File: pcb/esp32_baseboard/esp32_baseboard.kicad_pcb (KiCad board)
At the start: 2 copper layers, 225 x 132 mm, 42 parts, among them J1 Screw_12V_IN, J10 LIM_MIN_NC, J11 LIM_MAX_NC, J12 LIM_MIN_NC, J13 LIM_MAX_NC, J14 BUP_30S, J15 BUZZER_5V, J16 AOD4184, J17 TFT_TOUCH, J18 EC11_ENC, J2 NEMA17_OUT, J4 OPTO_FIELD_IN, J5 GA12_N20, J6 GA12_N20, J7 GA12_N20, J8 LIM_MIN_NC, J9 LIM_MAX_NC, U1 ESP32_S3_DevKitC_1, U2 MP1584_5V3A, U3 TMC2209, U4 PC817_4CH, U5 DRV8871_Module, U6 DRV8871_Module, U7 DRV8871_Module, U9 PC817_4CH

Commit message: tmp
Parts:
- moved J5 213.6 mm to (265.0, 98.0), turned to 180 degrees
- moved J2 182.8 mm to (228.0, 65.8), turned to 180 degrees
- moved J6 166.3 mm to (265.0, 124.0), turned to 180 degrees
- moved J4 135.8 mm to (115.0, 132.0)
- moved J7 130.0 mm to (265.0, 150.0), turned to 180 degrees
- moved J11 62.0 mm to (61.0, 72.0)
- moved U3 50.0 mm to (247.0, 62.0)
- moved J10 46.0 mm to (69.0, 72.0)
- moved J14 45.2 mm to (200.0, 58.0)
- moved R1 45.2 mm to (190.0, 66.1)
- moved C20 44.3 mm to (247.0, 78.0)
- moved C23 37.2 mm to (253.0, 159.0)
- moved J15 36.7 mm to (145.0, 58.0)
- moved C22 36.2 mm to (253.0, 133.0)
- moved U9 36.1 mm to (163.0, 141.0)
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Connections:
- net /BLOWER renamed BLOWER
- net /BLW_RET renamed BLW_RET
- net /DC1_IN1 renamed DC1_IN1
- net /DC1_IN2 renamed DC1_IN2
- net /DC2_IN1 renamed DC2_IN1
- net /DC2_IN2 renamed DC2_IN2
- net /DC3_IN1 renamed DC3_IN1
- net /DC3_IN2 renamed DC3_IN2
- net /DIR renamed DIR
- net /ENC_B renamed ENC_B
- net /EN_TMC renamed EN_TMC
- net /MotA1 renamed MotA1
- net /MotA2 renamed MotA2
- net /MotB1 renamed MotB1
- net /MotB2 renamed MotB2
- net /MotDC1_A renamed MotDC1_A
- net /MotDC1_B renamed MotDC1_B
- net /MotDC2_A renamed MotDC2_A
- net /MotDC2_B renamed MotDC2_B
- net /MotDC3_A renamed MotDC3_A
- net /MotDC3_B renamed MotDC3_B
- net /OPTO_IN1 renamed OPTO_IN1
- net /OPTO_IN2 renamed OPTO_IN2
- net /OPTO_IN3 renamed OPTO_IN3
- net /OPTO_IN4 renamed OPTO_IN4
- net /OPTO_IN5 renamed OPTO_IN5
- net /OPTO_IN6 renamed OPTO_IN6
- net /OPTO_IN7 renamed OPTO_IN7
- net /OPTO_IN8 renamed OPTO_IN8
- net /OPTO_OUT1 renamed OPTO_OUT1
- net /OPTO_OUT2 renamed OPTO_OUT2
- net /OPTO_OUT3 renamed OPTO_OUT3
- net /OPTO_OUT4 renamed OPTO_OUT4
- net /OPTO_OUT5 renamed OPTO_OUT5
- net /OPTO_OUT6 renamed OPTO_OUT6
- net /OPTO_OUT7 renamed OPTO_OUT7
- net /OPTO_OUT8 renamed OPTO_OUT8
- net /OPTO_VCC_I renamed OPTO_VCC_I
- net /STEP renamed STEP
- net /TFT_BL renamed TFT_BL
- net /TFT_CS renamed TFT_CS
- net /TFT_DC renamed TFT_DC
- net /TFT_MISO renamed TFT_MISO
- net /TFT_MOSI renamed TFT_MOSI
- net /TFT_RST renamed TFT_RST
- net /TFT_SCK renamed TFT_SCK
- net /T_CS renamed T_CS
- J14 pad 4: (no net) -> unconnected-(J14-CTRL-Pad4)
- J15 pad 3: /BUZZER -> BUZZER
- J18 pad 3: /ENC_A -> ENC_A
- U1 pad 15: /ENC_A -> BUZZER
- U1 pad 24: (no net) -> unconnected-(U1-TX0-Pad24)
- U1 pad 25: (no net) -> unconnected-(U1-RX0-Pad25)
- U1 pad 3: (no net) -> unconnected-(U1-RST-Pad3)
- U1 pad 32: /BUZZER -> ENC_A
- U1 pad 33: (no net) -> unconnected-(U1-IO37-Pad33)
- U1 pad 34: (no net) -> unconnected-(U1-IO36-Pad34)
- U1 pad 35: (no net) -> unconnected-(U1-IO35-Pad35)
- U1 pad 36: (no net) -> unconnected-(U1-IO0-Pad36)
- U1 pad 41: (no net) -> unconnected-(U1-IO20-Pad41)
- U1 pad 42: (no net) -> unconnected-(U1-IO19-Pad42)
- U3 pad 2: (no net) -> unconnected-(U3-MS1-Pad2)
- U3 pad 3: (no net) -> unconnected-(U3-MS2-Pad3)
- U3 pad 4: (no net) -> unconnected-(U3-PDN-Pad4)
- U3 pad 5: (no net) -> unconnected-(U3-PDN2-Pad5)
- U3 pad 6: (no net) -> unconnected-(U3-CLK-Pad6)
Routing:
- net GND: track 1179.7 -> 780.9 mm
- net TFT_MOSI: track 437.6 -> 61.2 mm
- net MotB1: track 378.9 -> 11.4 mm
- net OPTO_VCC_I: track 474.9 -> 111.9 mm
- net TFT_SCK: track 423.0 -> 61.2 mm
- net BLOWER: track 359.9 -> 72.5 mm, vias 0 -> 1
- net OPTO_IN7: track 412.5 -> 162.8 mm
- net MotDC3_B: track 255.0 -> 10.3 mm
- net OPTO_IN8: track 275.1 -> 42.1 mm
- net MotDC3_A: track 197.0 -> 8.00 mm
- net +5V: track 0.00 -> 142.2 mm
- net OPTO_IN1: track 270.5 -> 129.8 mm
- net +3V3: track 278.4 -> 417.2 mm, vias 0 -> 2
- net TFT_RST: track 0.00 -> 133.9 mm, vias 0 -> 2
- net DC3_IN2: track 0.00 -> 119.6 mm
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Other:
- board size 225 x 132 mm -> 235 x 132 mm
- net class Default removed
- net class Power removed
- board text added: "1 POWER J1/F1/D1/U2"
- board text added: "3 TMC U3"
- board text added: "5 DRV U5-U7"
- board text added: "B STEP J2 -> U3"
- board text added: "D FIELD J4"
- board text added: "E DC MOT J5-J7"
- board text added: "F LIMIT truc 1-2 (-> U4)"
- board text added: "F LIMIT truc 3 (-> U9)"
- board text added: "G BLW J16"
- board text added: "GND 3V3 A=IO38 B=IO41"
- board text added: "J5 GA12-N20 TRUC1"
- board text added: "J6 GA12-N20 TRUC2"
- board text added: "J7 GA12-N20 TRUC3"
- board text added: "T1 J8 MIN"
- board text added: "T1 J9 MAX"
- board text added: "T2 J10 MIN"
- board text added: "T2 J11 MAX"
- board text added: "T3 J12 MIN"
- board text added: "T3 J13 MAX"
- board text added: "TOP 235x132 — giac canh module dieu khien no"
- board text added: "U5 DRV8871 GA12 VM=12V"
- board text added: "U6 DRV8871 GA12 VM=12V"
- board text added: "U7 DRV8871 GA12 VM=12V"
- board text removed: "1 POWER J1/U2"
- board text removed: "3 TMC"
- board text removed: "B STEP"
- board text removed: "B.Cu bus"
- board text removed: "D SENSE"
- board text removed: "E+F DC MOT + LIMIT (cap truc)"
- board text removed: "G BLW"
- board text removed: "GND 3V3 A=IO9 B=IO41"
- board text removed: "J5 MOT J8 MIN J9 MAX"
- board text removed: "J6 MOT J10 MIN J11 MAX"
- board text removed: "J7 MOT J12 MIN J13 MAX"
- board text removed: "TOP 225x132 — giac theo nhom | BOTTOM module"
- board text removed: "TRUC1 MOT+LIM NC"
- board text removed: "TRUC2 MOT+LIM NC"
- board text removed: "TRUC3 MOT+LIM NC"
- board text removed: "U5 DRV8871 GA12"
- board text removed: "U6 DRV8871 GA12"
- board text removed: "U7 DRV8871 GA12"
- board text removed: "VM=12V"

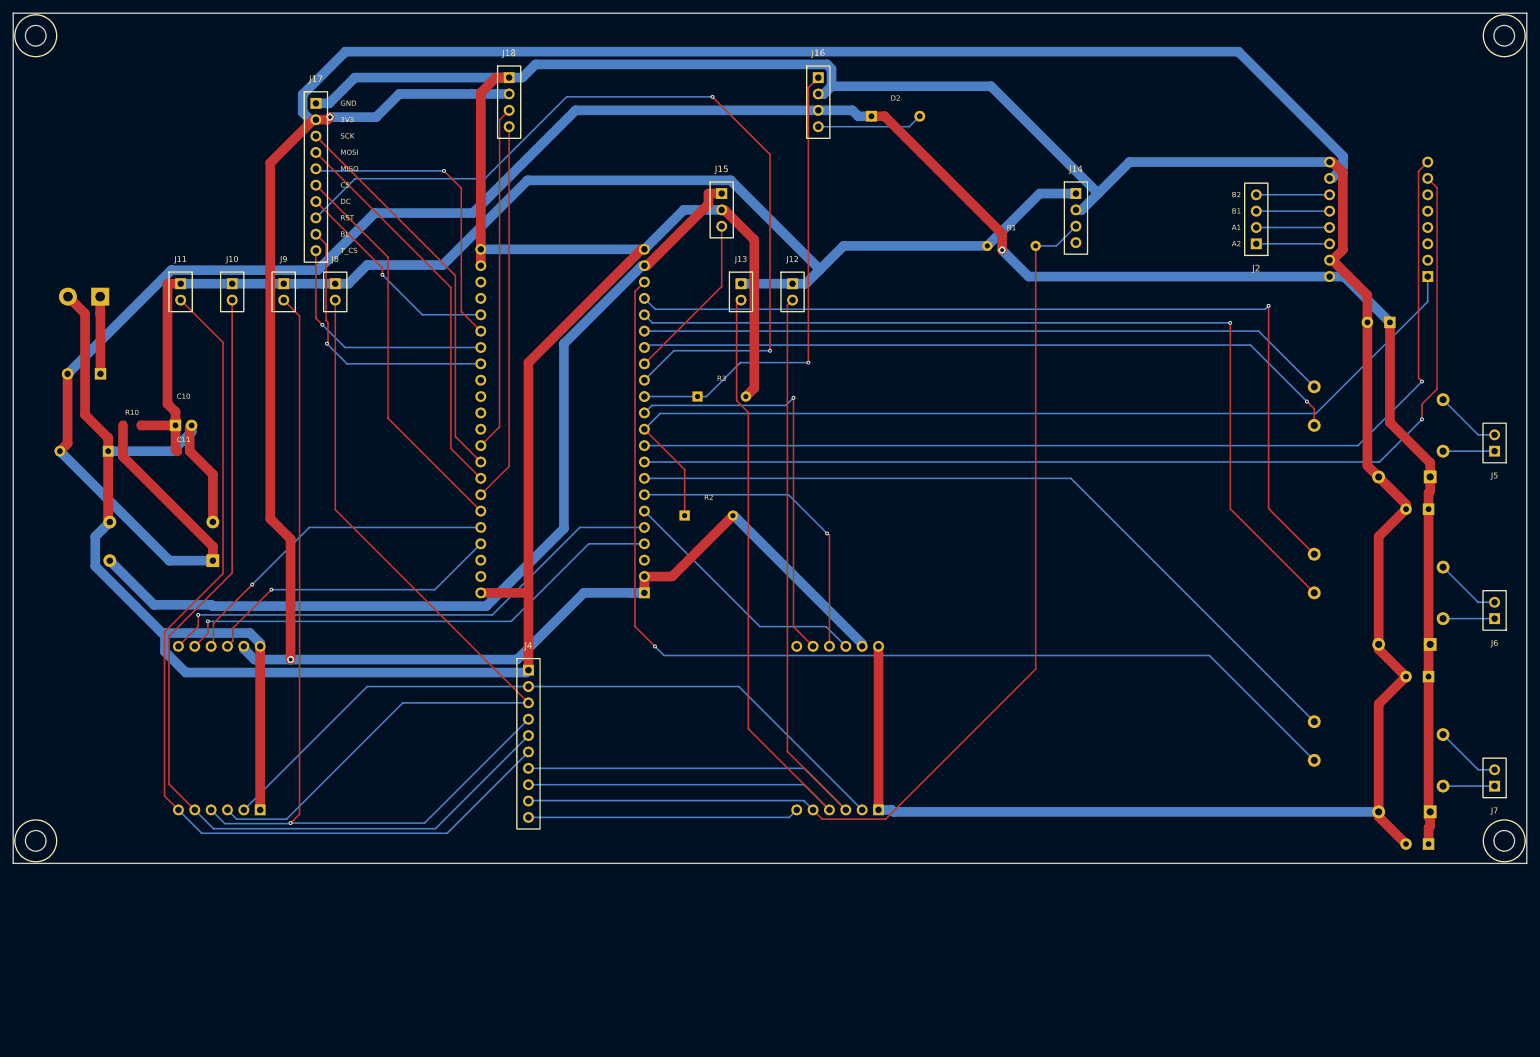
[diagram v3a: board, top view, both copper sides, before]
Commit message: sắp xếp và chọn lại linh kiện cho PCB
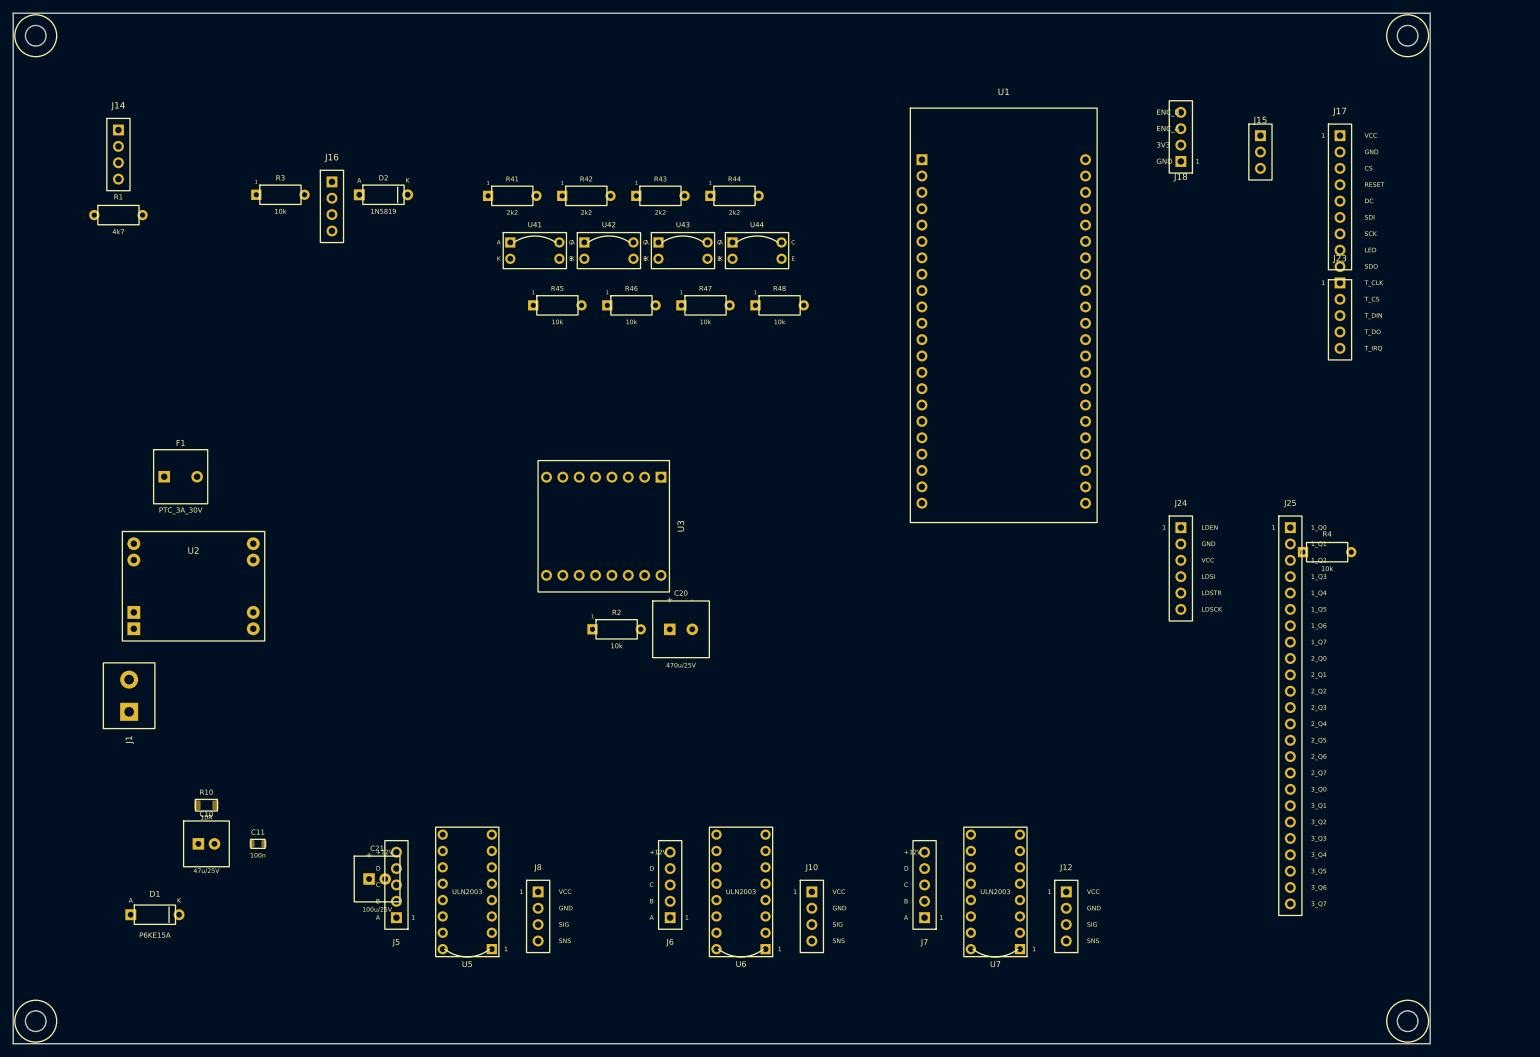
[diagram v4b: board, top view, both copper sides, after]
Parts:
- removed C22, C23: 470u/25V, ESP32_Carrier:CP_Radial_D8_470u_25V
- removed J11, J13, J9: LIM_MAX_NC, ESP32_Carrier:PinHeader_1x02_LimitSW
- removed J2: NEMA17_OUT, ESP32_Carrier:PinHeader_1x04_Motor
- removed J4: OPTO_FIELD_IN, ESP32_Carrier:PinHeader_1x10_OptoField
- removed U4, U9: PC817_4CH, ESP32_Carrier:PC817_4CH_Opto
- added J23: TFT_TP, ESP32_Carrier:PinHeader_1x05_TFT_TP, F.Cu at (241.0, 71.9)
- added J24: 595_CTRL, ESP32_Carrier:PinHeader_1x06_595CTRL, F.Cu at (216.3, 109.9)
- added J25: 595_Q, ESP32_Carrier:PinHeader_1x24_595Q, F.Cu at (233.3, 109.9)
- added R4: 10k, ESP32_Carrier:R_Axial_4k7_BUP, F.Cu at (239.0, 113.7)
- added R41: 2k2, ESP32_Carrier:R_Axial_4k7_BUP, F.Cu at (112.5, 58.4)
- added R42: 2k2, ESP32_Carrier:R_Axial_4k7_BUP, F.Cu at (124.0, 58.4)
- added R43: 2k2, ESP32_Carrier:R_Axial_4k7_BUP, F.Cu at (135.5, 58.4)
- added R44: 2k2, ESP32_Carrier:R_Axial_4k7_BUP, F.Cu at (147.0, 58.4)
- added R45: 10k, ESP32_Carrier:R_Axial_4k7_BUP, F.Cu at (119.5, 75.4)
- added R46: 10k, ESP32_Carrier:R_Axial_4k7_BUP, F.Cu at (131.0, 75.4)
- added R47: 10k, ESP32_Carrier:R_Axial_4k7_BUP, F.Cu at (142.5, 75.4)
- added R48: 10k, ESP32_Carrier:R_Axial_4k7_BUP, F.Cu at (154.0, 75.4)
- added U41: PC817, ESP32_Carrier:PC817_DIP4, F.Cu at (116.0, 66.9)
- added U42: PC817, ESP32_Carrier:PC817_DIP4, F.Cu at (127.5, 66.9)
- added U43: PC817, ESP32_Carrier:PC817_DIP4, F.Cu at (139.0, 66.9)
- added U44: PC817, ESP32_Carrier:PC817_DIP4, F.Cu at (150.5, 66.9)
- C20, D1, F1, J1, U1, U2, U3: moved to F.Cu
- C21: value 470u/25V -> 100u/25V; footprint ESP32_Carrier:CP_Radial_D8_470u_25V -> ESP32_Carrier:CP_Radial_D6_100u_25V; moved to F.Cu
- J10: value LIM_MIN_NC -> END_HOME2; footprint ESP32_Carrier:PinHeader_1x02_LimitSW -> ESP32_Carrier:PinHeader_1x04_Endstop
- J12: value LIM_MIN_NC -> END_HOME3; footprint ESP32_Carrier:PinHeader_1x02_LimitSW -> ESP32_Carrier:PinHeader_1x04_Endstop
- J17: value TFT_TOUCH -> TFT_LCD; footprint ESP32_Carrier:PinHeader_1x10_TFT -> ESP32_Carrier:PinHeader_1x09_TFT_LCD
- J5, J6, J7: value GA12_N20 -> 28BYJ48; footprint ESP32_Carrier:PinHeader_1x02_MotorDC -> ESP32_Carrier:PinHeader_1x05_BYJ
- J8: value LIM_MIN_NC -> END_HOME1; footprint ESP32_Carrier:PinHeader_1x02_LimitSW -> ESP32_Carrier:PinHeader_1x04_Endstop
- U5, U6, U7: value DRV8871_Module -> ULN2003AN; footprint ESP32_Carrier:DRV8871_Module -> ESP32_Carrier:ULN2003AN; moved to F.Cu
- moved J5 185.2 mm to (94.5, 170.4)
- moved C21 171.4 mm to (91.5, 164.4), turned to 0 degrees
- moved J17 159.1 mm to (241.0, 49.0)
- moved U5 159.0 mm to (105.5, 166.4)
- moved J14 149.0 mm to (51.3, 48.1)
- moved R1 138.7 mm to (51.3, 61.3)
- moved J6 136.2 mm to (137.0, 170.4)
- moved J10 130.4 mm to (159.0, 166.4)
- moved U3 129.4 mm to (126.7, 109.7), turned to 270 degrees
- moved C20 118.3 mm to (138.7, 125.7), turned to 0 degrees
- moved U6 109.3 mm to (148.0, 166.4)
- moved J18 105.1 mm to (216.3, 53.0), turned to 180 degrees
- moved J12 103.5 mm to (198.5, 166.4)
- moved J8 99.5 mm to (116.5, 166.4)
- moved J7 90.8 mm to (176.5, 170.4)
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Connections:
- J10 pad 1: +12V_SNS -> (no net)
- J10 pad 2: OPTO_IN3 -> (no net)
- J12 pad 1: +12V_SNS -> (no net)
- J12 pad 2: OPTO_IN5 -> (no net)
- J14 pad 3: OPTO_IN7 -> OPTO_IN4
- J14 pad 4: unconnected-(J14-CTRL-Pad4) -> (no net)
- J17 pad 1: GND -> +3V3
- J17 pad 2: +3V3 -> GND
- J17 pad 3: TFT_SCK -> TFT_CS
- J17 pad 4: TFT_MOSI -> TFT_RST
- J17 pad 5: TFT_MISO -> TFT_DC
- J17 pad 6: TFT_CS -> TFT_MOSI
- J17 pad 7: TFT_DC -> TFT_SCK
- J17 pad 8: TFT_RST -> TFT_BL
- J17 pad 9: TFT_BL -> (no net)
- J5 pad 1: MotDC1_A -> BYJ1_A
- J5 pad 2: MotDC1_B -> BYJ1_B
- J6 pad 1: MotDC2_A -> BYJ2_A
- J6 pad 2: MotDC2_B -> BYJ2_B
- J7 pad 1: MotDC3_A -> BYJ3_A
- J7 pad 2: MotDC3_B -> BYJ3_B
- J8 pad 1: +12V_SNS -> (no net)
- J8 pad 2: OPTO_IN1 -> (no net)
- R1 pad 2: OPTO_IN7 -> OPTO_IN4
- U1 pad 12: OPTO_OUT7 -> (no net)
- U1 pad 16: DC1_IN1 -> SER
- U1 pad 17: DC1_IN2 -> SRCLK
- U1 pad 18: DC2_IN1 -> RCLK
- U1 pad 19: DC2_IN2 -> OE_595
- U1 pad 20: DC3_IN1 -> (no net)
- U1 pad 24: unconnected-(U1-TX0-Pad24) -> (no net)
- U1 pad 25: unconnected-(U1-RX0-Pad25) -> (no net)
- U1 pad 3: unconnected-(U1-RST-Pad3) -> (no net)
- U1 pad 33: unconnected-(U1-IO37-Pad33) -> (no net)
- U1 pad 34: unconnected-(U1-IO36-Pad34) -> (no net)
- U1 pad 35: unconnected-(U1-IO35-Pad35) -> (no net)
- U1 pad 36: unconnected-(U1-IO0-Pad36) -> (no net)
- U1 pad 41: unconnected-(U1-IO20-Pad41) -> (no net)
- U1 pad 42: unconnected-(U1-IO19-Pad42) -> (no net)
- U1 pad 6: OPTO_OUT5 -> T_IRQ
- U1 pad 7: OPTO_OUT6 -> (no net)
- U1 pad 8: DC3_IN2 -> (no net)
- U2 pad 3: +5V -> GND
- U2 pad 4: GND -> +5V
- U3 pad 2: unconnected-(U3-MS1-Pad2) -> (no net)
- U3 pad 3: unconnected-(U3-MS2-Pad3) -> (no net)
- U3 pad 4: unconnected-(U3-PDN-Pad4) -> (no net)
- U3 pad 5: unconnected-(U3-PDN2-Pad5) -> (no net)
- U3 pad 6: unconnected-(U3-CLK-Pad6) -> (no net)
- U5 pad 1: +12V -> SR_Q0
- U5 pad 2: GND -> SR_Q1
- U5 pad 3: DC1_IN1 -> SR_Q2
- U5 pad 4: DC1_IN2 -> SR_Q3
- U5 pad 5: MotDC1_A -> (no net)
- U5 pad 6: MotDC1_B -> (no net)
- U6 pad 1: +12V -> SR_Q4
- U6 pad 2: GND -> SR_Q5
- U6 pad 3: DC2_IN1 -> SR_Q6
- U6 pad 4: DC2_IN2 -> SR_Q7
- U6 pad 5: MotDC2_A -> (no net)
- U6 pad 6: MotDC2_B -> (no net)
- U7 pad 1: +12V -> SR_Q8
- U7 pad 2: GND -> SR_Q9
- U7 pad 3: DC3_IN1 -> SR_Q10
- U7 pad 4: DC3_IN2 -> SR_Q11
- U7 pad 5: MotDC3_A -> (no net)
- U7 pad 6: MotDC3_B -> (no net)
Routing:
- net GND: track 780.9 -> 0.00 mm
- net +3V3: track 417.2 -> 0.00 mm, vias 2 -> 0
- net +12V: track 392.7 -> 0.00 mm, vias 1 -> 0
- net +12V_SNS: track 203.5 -> 0.00 mm
- net DC3_IN1: track 168.2 -> 0.00 mm, vias 1 -> 0
- net OPTO_IN7: track 162.8 -> 0.00 mm
- net STEP: track 162.5 -> 0.00 mm, vias 1 -> 0
- net DIR: track 159.7 -> 0.00 mm, vias 1 -> 0
- net EN_TMC: track 149.7 -> 0.00 mm
- net OPTO_IN4: track 147.6 -> 0.00 mm
- net OPTO_IN3: track 143.9 -> 0.00 mm
- net +5V: track 142.2 -> 0.00 mm
- net OPTO_IN2: track 139.7 -> 0.00 mm, vias 1 -> 0
- net DC2_IN2: track 139.3 -> 0.00 mm, vias 1 -> 0
- net DC2_IN1: track 138.8 -> 0.00 mm, vias 1 -> 0
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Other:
- board size 235 x 132 mm -> 220 x 160 mm
- net class Default added: clearance 0.2, trace_width 0.25, via_dia 0.8, via_drill 0.4
- net class Power added: clearance 0.25, trace_width 1.00, via_dia 1.1, via_drill 0.6
- board text added: "1: POWER J1+F1+D1+U2+RC"
- board text added: "2: MCU U1 ESP32-S3 DevKitC"
- board text added: "3: TMC U3 + Mot pins (NEMA17 on module)"
- board text added: "4: OPTO U41-U44 PC817 + R2k2/10k"
- board text added: "5: SHIFT U10 595-24IO + J24/J25 + R4"
- board text added: "A1: HOME1+U5+J5"
- board text added: "A2: HOME2+U6+J6"
- board text added: "A3: HOME3+U7+J7"
- board text added: "All parts TOP (F.Cu); B.Cu = routing only. Eco1 cluster = cyan"
- board text added: "B: BLOWER J16 AOD4184 + R3/D2"
- board text added: "C20 470u/25V TMC"
- board text added: "C21 100u/25V ULN"
- board text added: "C: HMI J17 LCD + J23 TP + J18 ENC + J15 BZ"
- board text added: "J10 HOME2"
- board text added: "J12 HOME3"
- board text added: "J5 28BYJ BYJ1"
- board text added: "J6 28BYJ BYJ2"
- board text added: "J7 28BYJ BYJ3"
- board text added: "J8 HOME1"
- board text added: "LCD"
- board text added: "OPTO PC817x8 + 2k2/10k"
- board text added: "R4 LDEN/OE pull-up 10k"
- board text added: "R41 LED HOME1"
- board text added: "R42 LED HOME2"
- board text added: "R43 LED HOME3"
- board text added: "R44 LED BUP"
- board text added: "R45 PU HOME1"
- board text added: "R46 PU HOME2"
- board text added: "R47 PU HOME3"
- board text added: "R48 PU BUP"
- board text added: "Shopee thegioimodule 3x595"
- board text added: "TP"
- board text added: "U10 74HC595-24IO module"
- board text added: "U: BUP-30S J14 + R1 4k7"
- board text removed: "1 POWER J1/F1/D1/U2"
- board text removed: "2 MCU U1"
- board text removed: "2x PC817 4CH | OUT=MCU IN=J4 field"
- board text removed: "3 TMC U3"
- board text removed: "5 DRV U5-U7"
- board text removed: "B STEP J2 -> U3"
- board text removed: "BOTTOM — 1 POWER | 2 MCU | 3 TMC | 4 OPTO | 5 DRV"
- board text removed: "C HMI J17/J18/J15"
- board text removed: "C20 470u TMC"
- board text removed: "C21 470u U5"
- board text removed: "C22 470u U6"
- board text removed: "C23 470u U7"
- board text removed: "D FIELD J4"
- board text removed: "E DC MOT J5-J7"
- board text removed: "F LIMIT truc 1-2 (-> U4)"
- board text removed: "F LIMIT truc 3 (-> U9)"
- board text removed: "G BLW J16"
- board text removed: "IN1-6=lim; IN7=BUP30S; IN8 free"
- board text removed: "J4 OPTO FIELD IN"
- board text removed: "J5 GA12-N20 TRUC1"
- board text removed: "J6 GA12-N20 TRUC2"
- board text removed: "J7 GA12-N20 TRUC3"
- board text removed: "T1 J8 MIN"
- board text removed: "T1 J9 MAX"
- board text removed: "T2 J10 MIN"
- board text removed: "T2 J11 MAX"
- board text removed: "T3 J12 MIN"
- board text removed: "T3 J13 MAX"
- board text removed: "TOP 235x132 — giac canh module dieu khien no"
- board text removed: "U4 PC817 4CH"
- board text removed: "U5 DRV8871 GA12 VM=12V"
- board text removed: "U6 DRV8871 GA12 VM=12V"
- board text removed: "U7 DRV8871 GA12 VM=12V"
- board text removed: "U9 PC817 4CH"

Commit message: đi dây cho mạch PCB
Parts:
- moved R4 19.7 mm to (222.5, 102.9)
- moved C21 12.0 mm to (91.5, 152.4)
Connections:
- J10 pad 1: (no net) -> unconnected-(J10-VCC-Pad1)
- J10 pad 2: (no net) -> unconnected-(J10-GND-Pad2)
- J12 pad 1: (no net) -> unconnected-(J12-VCC-Pad1)
- J12 pad 2: (no net) -> unconnected-(J12-GND-Pad2)
- J14 pad 4: (no net) -> unconnected-(J14-CTRL-Pad4)
- J17 pad 9: (no net) -> unconnected-(J17-SDO-Pad9)
- J25 pad 13: (no net) -> unconnected-(J25-P13-Pad13)
- J25 pad 14: (no net) -> unconnected-(J25-P14-Pad14)
- J25 pad 15: (no net) -> unconnected-(J25-P15-Pad15)
- J25 pad 16: (no net) -> unconnected-(J25-P16-Pad16)
- J25 pad 17: (no net) -> unconnected-(J25-P17-Pad17)
- J25 pad 18: (no net) -> unconnected-(J25-P18-Pad18)
- J25 pad 19: (no net) -> unconnected-(J25-P19-Pad19)
- J25 pad 20: (no net) -> unconnected-(J25-P20-Pad20)
- J25 pad 21: (no net) -> unconnected-(J25-P21-Pad21)
- J25 pad 22: (no net) -> unconnected-(J25-P22-Pad22)
- J25 pad 23: (no net) -> unconnected-(J25-P23-Pad23)
- J25 pad 24: (no net) -> unconnected-(J25-P24-Pad24)
- J8 pad 1: (no net) -> unconnected-(J8-VCC-Pad1)
- J8 pad 2: (no net) -> unconnected-(J8-GND-Pad2)
- U1 pad 12: (no net) -> unconnected-(U1-IO8-Pad12)
- U1 pad 20: (no net) -> unconnected-(U1-IO14-Pad20)
- U1 pad 24: (no net) -> unconnected-(U1-TX0-Pad24)
- U1 pad 25: (no net) -> unconnected-(U1-RX0-Pad25)
- U1 pad 3: (no net) -> unconnected-(U1-RST-Pad3)
- U1 pad 33: (no net) -> unconnected-(U1-IO37-Pad33)
- U1 pad 34: (no net) -> unconnected-(U1-IO36-Pad34)
- U1 pad 35: (no net) -> unconnected-(U1-IO35-Pad35)
- U1 pad 36: (no net) -> unconnected-(U1-IO0-Pad36)
- U1 pad 41: (no net) -> unconnected-(U1-IO20-Pad41)
- U1 pad 42: (no net) -> unconnected-(U1-IO19-Pad42)
- U1 pad 7: (no net) -> unconnected-(U1-IO7-Pad7)
- U1 pad 8: (no net) -> unconnected-(U1-IO15-Pad8)
- U3 pad 2: (no net) -> unconnected-(U3-MS1-Pad2)
- U3 pad 3: (no net) -> unconnected-(U3-MS2-Pad3)
- U3 pad 4: (no net) -> unconnected-(U3-PDN-Pad4)
- U3 pad 5: (no net) -> unconnected-(U3-PDN2-Pad5)
- U3 pad 6: (no net) -> unconnected-(U3-CLK-Pad6)
- U5 pad 10: (no net) -> unconnected-(U5-OUT7-Pad10)
- U5 pad 11: (no net) -> unconnected-(U5-OUT6-Pad11)
- U5 pad 12: (no net) -> unconnected-(U5-OUT5-Pad12)
- U5 pad 5: (no net) -> unconnected-(U5-IN5-Pad5)
- U5 pad 6: (no net) -> unconnected-(U5-IN6-Pad6)
- U5 pad 7: (no net) -> unconnected-(U5-IN7-Pad7)
- U6 pad 10: (no net) -> unconnected-(U6-OUT7-Pad10)
- U6 pad 11: (no net) -> unconnected-(U6-OUT6-Pad11)
- U6 pad 12: (no net) -> unconnected-(U6-OUT5-Pad12)
- U6 pad 5: (no net) -> unconnected-(U6-IN5-Pad5)
- U6 pad 6: (no net) -> unconnected-(U6-IN6-Pad6)
- U6 pad 7: (no net) -> unconnected-(U6-IN7-Pad7)
- U7 pad 10: (no net) -> unconnected-(U7-OUT7-Pad10)
- U7 pad 11: (no net) -> unconnected-(U7-OUT6-Pad11)
- U7 pad 12: (no net) -> unconnected-(U7-OUT5-Pad12)
- U7 pad 5: (no net) -> unconnected-(U7-IN5-Pad5)
- U7 pad 6: (no net) -> unconnected-(U7-IN6-Pad6)
- U7 pad 7: (no net) -> unconnected-(U7-IN7-Pad7)
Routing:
- net GND: track 0.00 -> 696.4 mm, vias 0 -> 1
- net +12V: track 0.00 -> 385.4 mm, vias 0 -> 1
- net +3V3: track 0.00 -> 288.3 mm, vias 0 -> 1
- net +12V_SNS: track 0.00 -> 283.4 mm
- net +5V: track 0.00 -> 236.6 mm, vias 0 -> 1
- net SR_Q0: track 0.00 -> 168.3 mm, vias 0 -> 1
- net SR_Q1: track 0.00 -> 166.6 mm, vias 0 -> 1
- net OPTO_IN3: track 0.00 -> 159.9 mm, vias 0 -> 1
- net SR_Q2: track 0.00 -> 157.9 mm, vias 0 -> 1
- net SR_Q3: track 0.00 -> 157.0 mm, vias 0 -> 2
- net SR_Q4: track 0.00 -> 142.4 mm, vias 0 -> 2
- net BLOWER: track 0.00 -> 138.3 mm, vias 0 -> 1
- net OPTO_IN2: track 0.00 -> 130.7 mm
- net OPTO_OUT1: track 0.00 -> 124.3 mm, vias 0 -> 1
- net T_IRQ: track 0.00 -> 118.5 mm, vias 0 -> 2
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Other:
- net class Default removed
- net class Power removed
